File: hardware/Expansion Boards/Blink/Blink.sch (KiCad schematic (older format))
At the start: 13 parts, among them J1 Daughter Board Connector

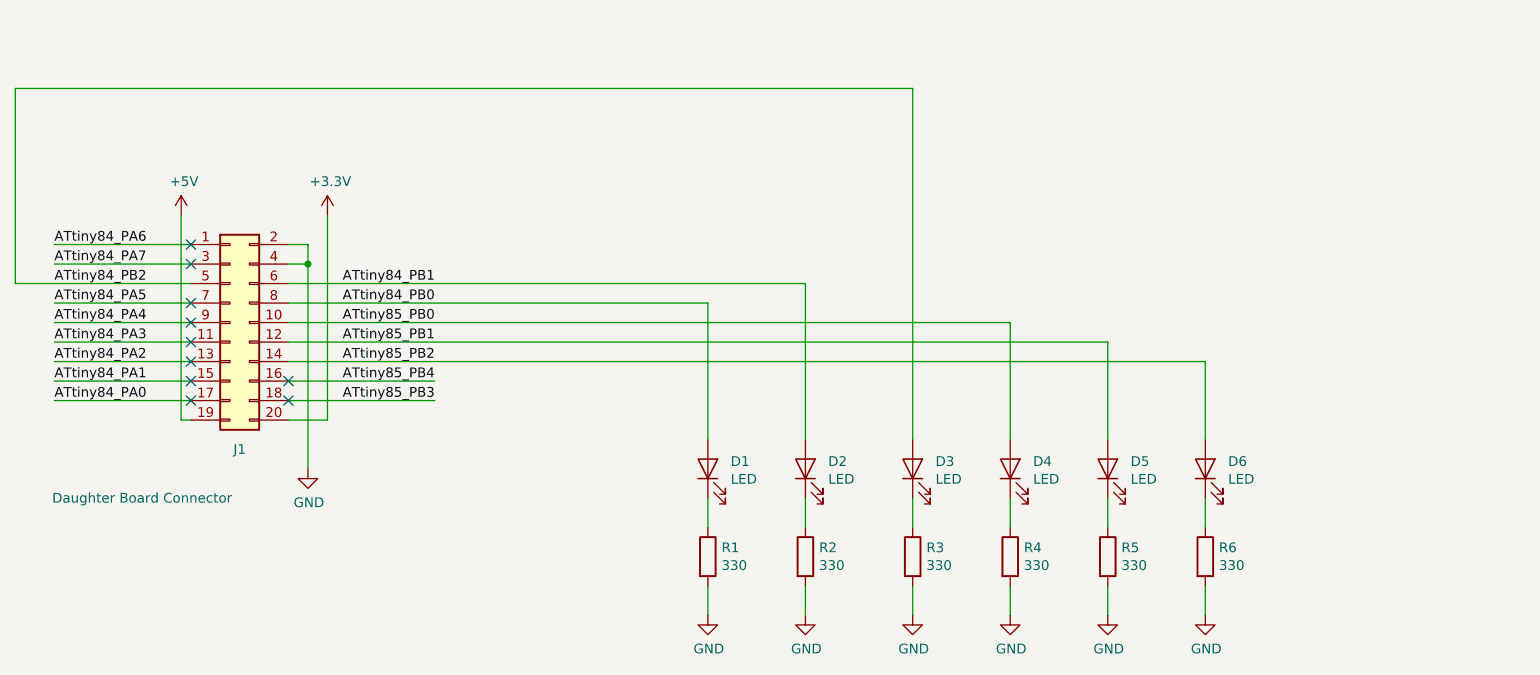
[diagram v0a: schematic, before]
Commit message: New Blink Expansion Board
Signed-off-by: John Jacques <eruditelite@gmail.com>
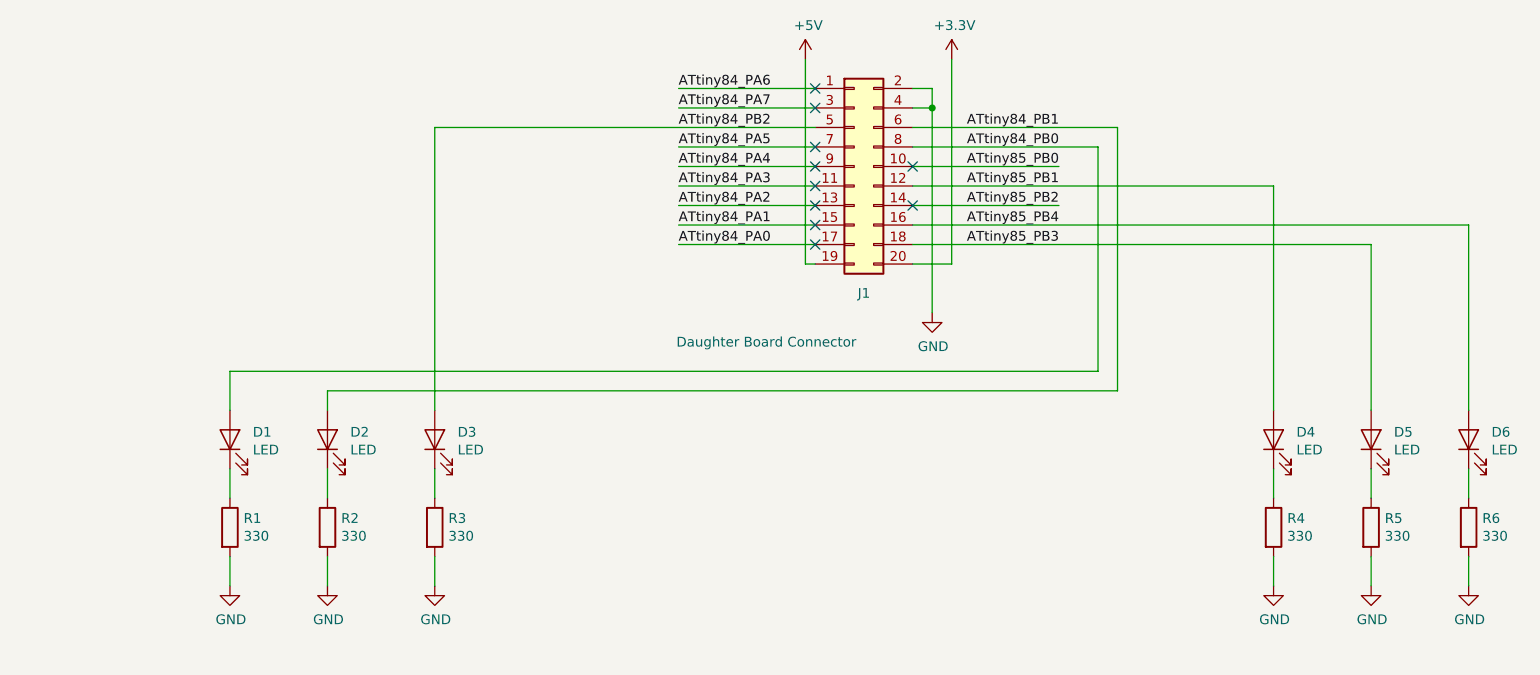
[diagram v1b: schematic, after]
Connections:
- net ATtiny85_PB0: no longer D4.2 (A)
- net ATtiny85_PB1: now also D4.2 (A); no longer D5.2 (A)
- net ATtiny85_PB2: no longer D6.2 (A)
- net ATtiny85_PB3: now also D5.2 (A)
- net ATtiny85_PB4: now also D6.2 (A)
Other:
- moved on the sheet: D1, D2, D3, D4, D5, D6, J1, R1, R2, R3, R4, R5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
